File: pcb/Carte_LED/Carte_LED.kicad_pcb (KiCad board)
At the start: 2 copper layers, 50 x 37.5 mm, 13 parts, among them J1 Conn_01x02

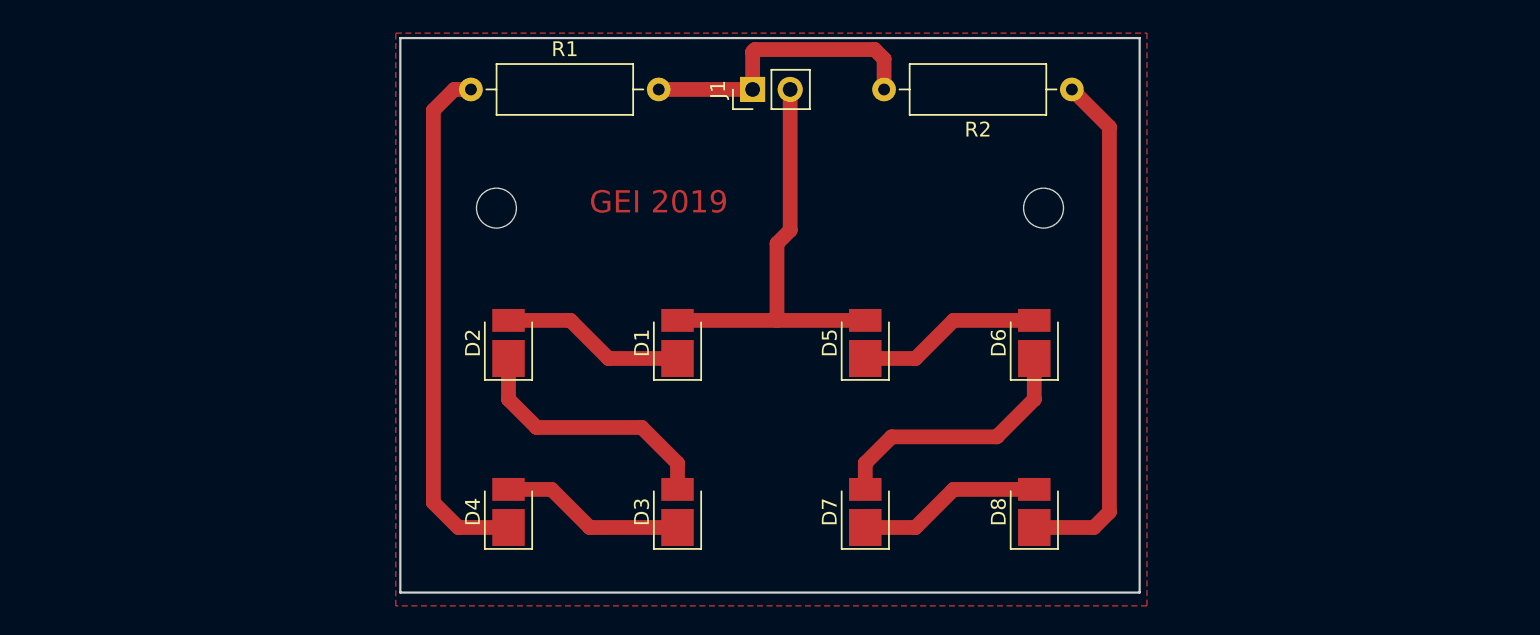
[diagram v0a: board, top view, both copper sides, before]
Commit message: ajout de la carte chassi DFRobotics + creation d'une nouvelle carte led + creation d'une carte capteur pour DFRobotic + correction de l'alimentation en 5V des encodeurs sur DFRobotic (carte Landzo a corriger dans un prochaine commit)
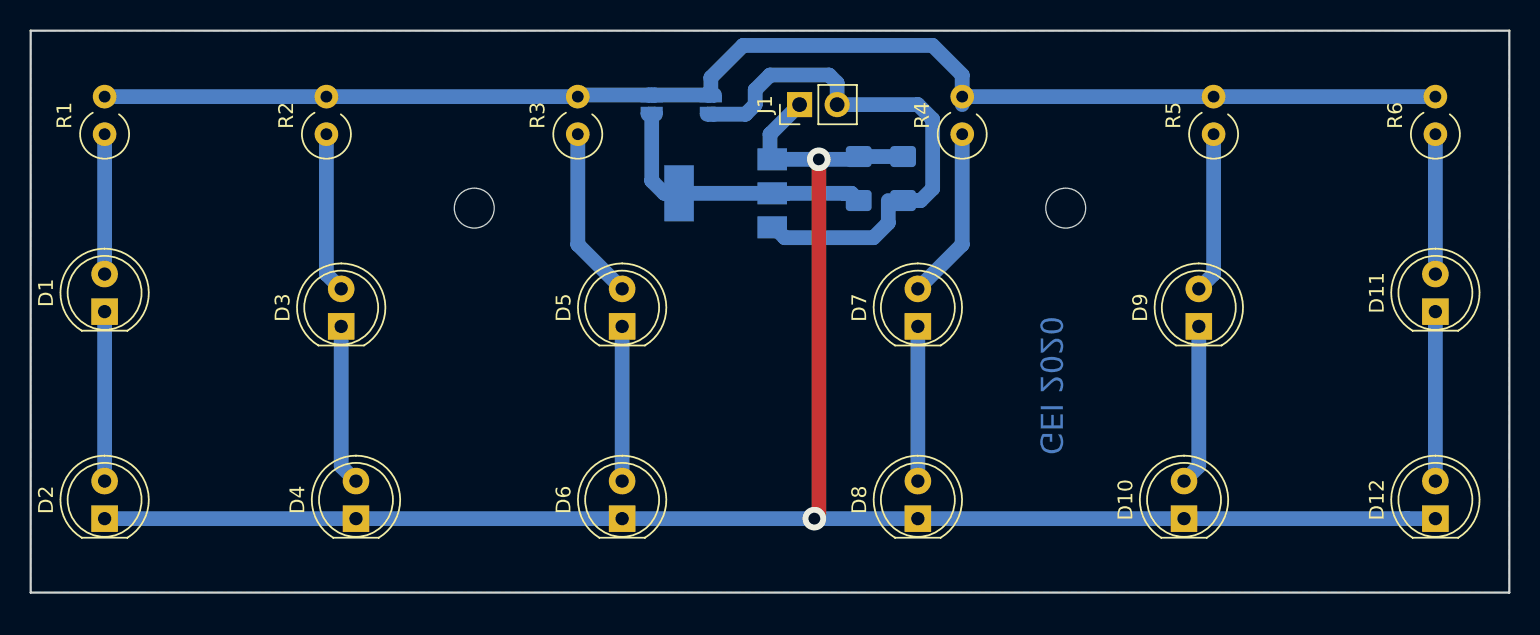
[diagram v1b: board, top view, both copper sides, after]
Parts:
- added C1: 4.7µF, Capacitor_SMD:C_1206_3216Metric_Pad1.42x1.75mm_HandSolder, B.Cu at (134.0, 60.0)
- added C2: 4.7µF, Capacitor_SMD:C_1206_3216Metric_Pad1.42x1.75mm_HandSolder, B.Cu at (131.0, 60.0)
- added D10: VLCS5830, LED_THT:LED_D5.0mm_Clear, F.Cu at (153.0, 83.0)
- added D11: VLCS5830, LED_THT:LED_D5.0mm_Clear, F.Cu at (170.0, 69.0)
- added D12: VLCS5830, LED_THT:LED_D5.0mm_Clear, F.Cu at (170.0, 83.0)
- added D9: VLCS5830, LED_THT:LED_D5.0mm_Clear, F.Cu at (154.0, 70.0)
- added JP1: SolderJumper_2_Open, Jumper:SolderJumper-2_P1.3mm_Open_RoundedPad1.0x1.5mm, B.Cu at (121.0, 55.0)
- added JP2: SolderJumper_2_Open, Jumper:SolderJumper-2_P1.3mm_Open_RoundedPad1.0x1.5mm, B.Cu at (117.0, 55.0)
- added R3: 10R, Resistor_THT:R_Axial_DIN0309_L9.0mm_D3.2mm_P2.54mm_Vertical, F.Cu at (112.0, 57.0)
- added R4: 10R, Resistor_THT:R_Axial_DIN0309_L9.0mm_D3.2mm_P2.54mm_Vertical, F.Cu at (138.0, 57.0)
- added R5: 10R, Resistor_THT:R_Axial_DIN0309_L9.0mm_D3.2mm_P2.54mm_Vertical, F.Cu at (155.0, 57.0)
- added R6: 10R, Resistor_THT:R_Axial_DIN0309_L9.0mm_D3.2mm_P2.54mm_Vertical, F.Cu at (170.0, 57.0)
- added U1: ZLDO1117G50TA, Package_TO_SOT_SMD:SOT-223-3_TabPin2, B.Cu at (122.0, 61.0)
- D1, D2, D3, D4, D5, D6, D7, D8: value L1SP-FRD00035R0000 -> VLCS5830; footprint LED_SMD:LED_PLCC_2835_Handsoldering -> LED_THT:LED_D5.0mm_Clear
- R1, R2: value R -> 10R; footprint Resistor_THT:R_Axial_DIN0309_L9.0mm_D3.2mm_P12.70mm_Horizontal -> Resistor_THT:R_Axial_DIN0309_L9.0mm_D3.2mm_P2.54mm_Vertical
- moved R2 50.5 mm to (95.0, 57.0), turned to 90 degrees
- moved D1 38.8 mm to (80.0, 69.0)
- moved D6 30.3 mm to (115.0, 83.0)
- moved D2 29.8 mm to (80.0, 83.0)
- moved D3 26.0 mm to (96.0, 70.0)
- moved R1 25.0 mm to (80.0, 57.0), turned to 90 degrees
- moved D5 16.5 mm to (115.0, 70.0)
- moved D7 13.0 mm to (135.0, 70.0)
- moved D4 10.3 mm to (97.0, 83.0)
- moved D8 7.89 mm to (135.0, 83.0)
- moved J1 3.34 mm to (127.0, 55.0)
- moved H1 1.50 mm to (105.0, 62.0)
- moved H2 1.50 mm to (145.0, 62.0)
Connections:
- D1 pad 2: +BATT -> Net-(D1-Pad2)
- D2 pad 1: Net-(D2-Pad1) -> GND
- D3 pad 2: Net-(D2-Pad1) -> Net-(D3-Pad2)
- D4 pad 1: Net-(D4-Pad1) -> GND
- D5 pad 2: +BATT -> Net-(D5-Pad2)
- D6 pad 1: Net-(D6-Pad1) -> GND
- D7 pad 2: Net-(D6-Pad1) -> Net-(D7-Pad2)
- D8 pad 1: Net-(D8-Pad1) -> GND
- R1 pad 1: Net-(D4-Pad1) -> Net-(D1-Pad2)
- R1 pad 2: GND -> +5V
- R2 pad 1: Net-(D8-Pad1) -> Net-(D3-Pad2)
- R2 pad 2: GND -> +5V
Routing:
- net GND: track 20.2 -> 128.2 mm, vias 0 -> 2
- net +5V: track 0.00 -> 94.9 mm
- net Net-(D4-Pad1): track 35.4 -> 0.00 mm
- net Net-(D8-Pad1): track 35.1 -> 0.00 mm
- net Net-(C2-Pad1): track 0.00 -> 19.1 mm
- net Net-(D6-Pad1): track 17.8 -> 0.00 mm
- net Net-(D2-Pad1): track 17.8 -> 0.00 mm
- net Net-(D7-Pad2): track 0.00 -> 11.7 mm
- net Net-(D5-Pad2): track 0.00 -> 11.7 mm
- net Net-(D11-Pad1): track 0.00 -> 11.5 mm
- net Net-(D9-Pad2): track 0.00 -> 10.9 mm
- net Net-(D3-Pad2): track 0.00 -> 10.9 mm
- net Net-(D10-Pad2): track 0.00 -> 10.9 mm
- net Net-(D11-Pad2): track 0.00 -> 9.46 mm
- net Net-(D1-Pad2): track 0.00 -> 9.46 mm
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- added copper zone on B.Cu, net GND
- removed copper zone on F.Cu, net GND
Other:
- board size 50 x 37.5 mm -> 100 x 38 mm
- board text added: "GEI 2020"
- board text removed: "GEI 2019"
